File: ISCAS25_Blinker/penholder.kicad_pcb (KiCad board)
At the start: 2 copper layers, 85 x 16.1 mm, 10 parts

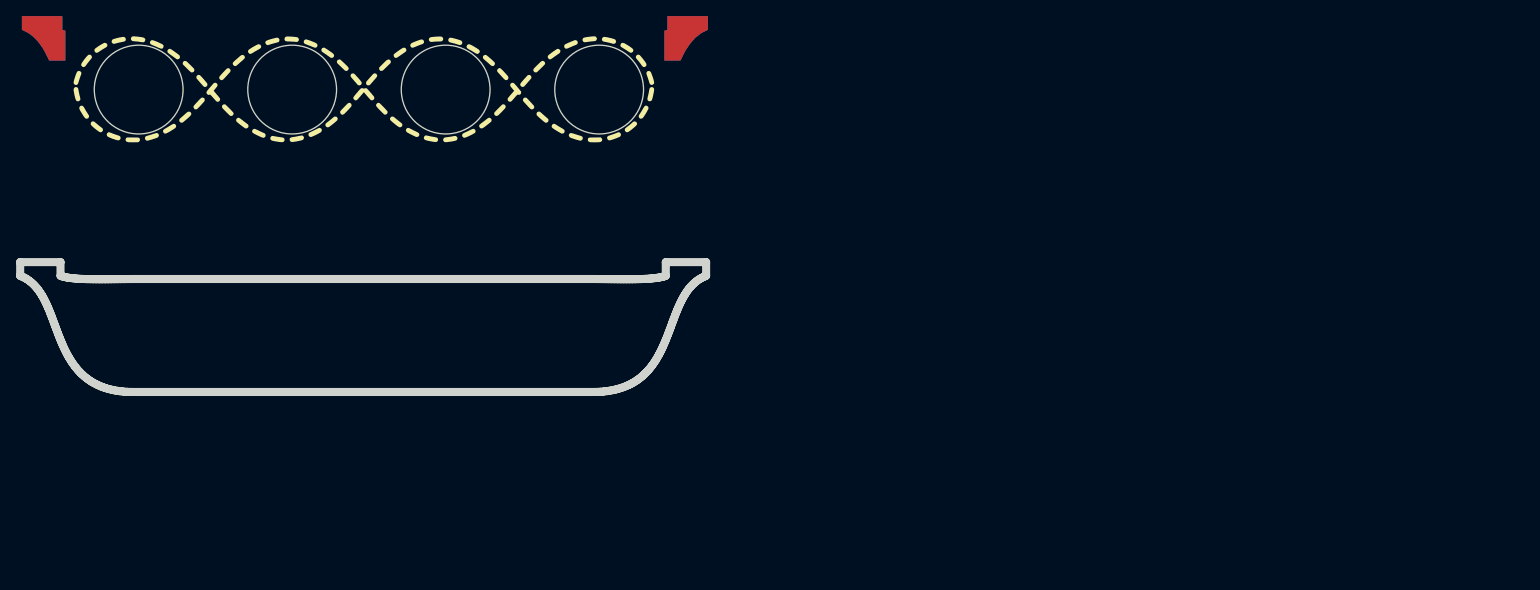
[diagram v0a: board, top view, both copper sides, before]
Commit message: Schematic done
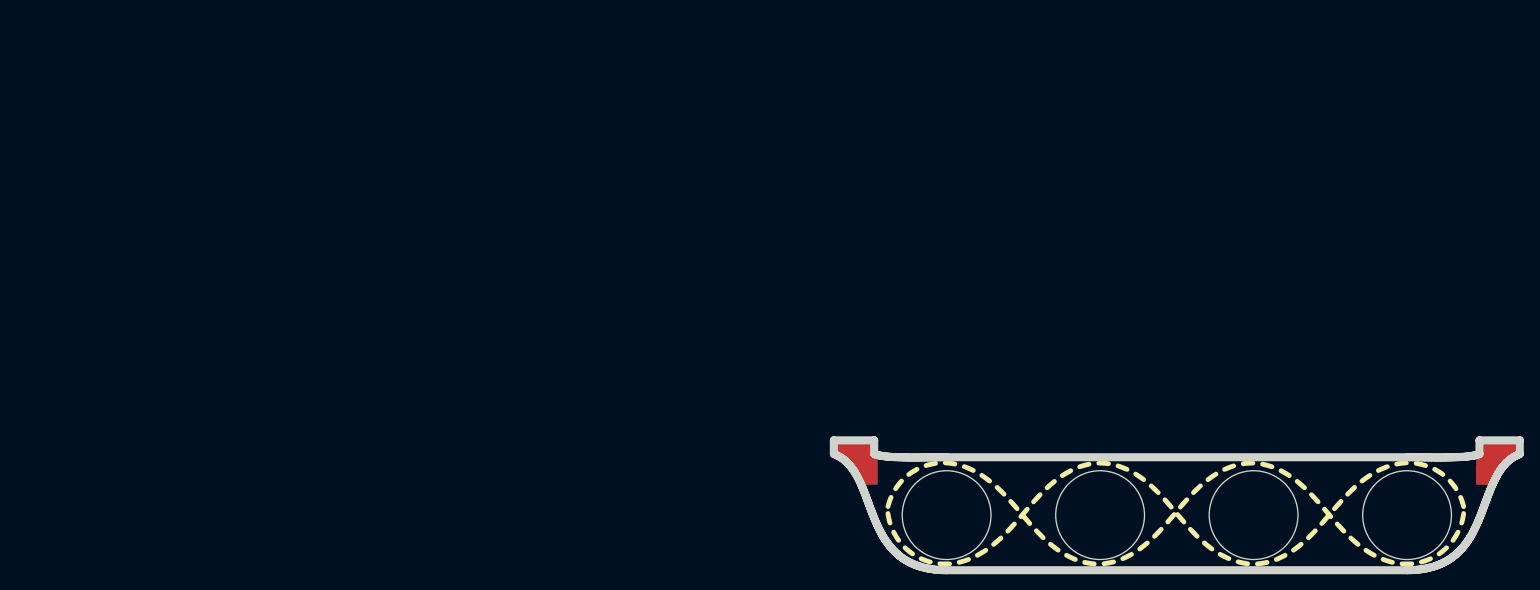
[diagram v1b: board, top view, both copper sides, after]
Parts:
- ? (x4): moved to F.Cu
- moved ? 142.9 mm to (108.1, 93.5) (x6)
- moved ? 113.2 mm to (160.1, 102.7)
- moved ? 113.2 mm to (122.1, 102.7)
- moved ? 113.2 mm to (179.2, 102.7)
- moved ? 113.2 mm to (141.1, 102.7)
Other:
- outline, holes or cut-outs redrawn
